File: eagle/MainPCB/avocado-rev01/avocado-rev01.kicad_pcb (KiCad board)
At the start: 2 copper layers, 61.5 x 60 mm, 85 parts, among them J1 10118194-0001LF, J3 0475710001, P2 camconn, U1 V3S, U2 AP65111A, U3 AP65111A, U4 AP65111A, X1 XTAL3.2X2, X2 XTAL5X1.9

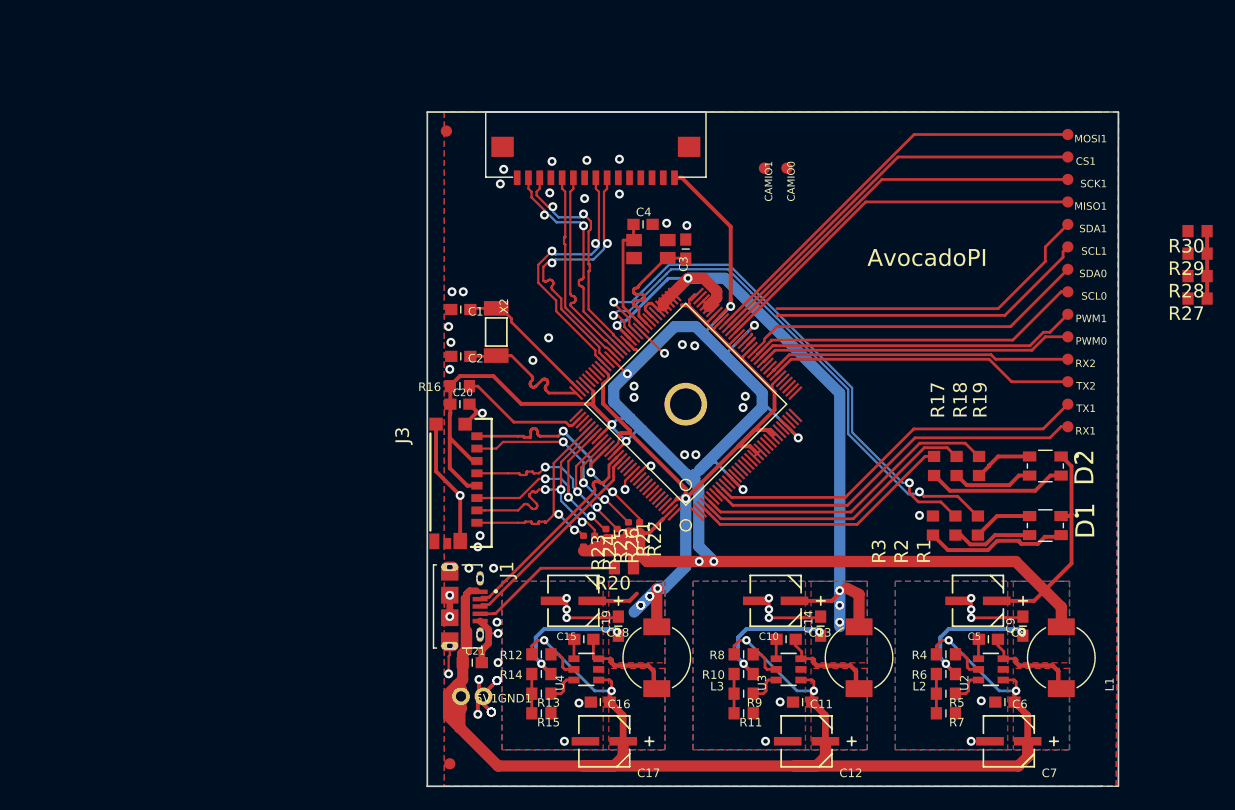
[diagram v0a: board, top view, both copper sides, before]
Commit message: accurate high speed routing, now 4 layer
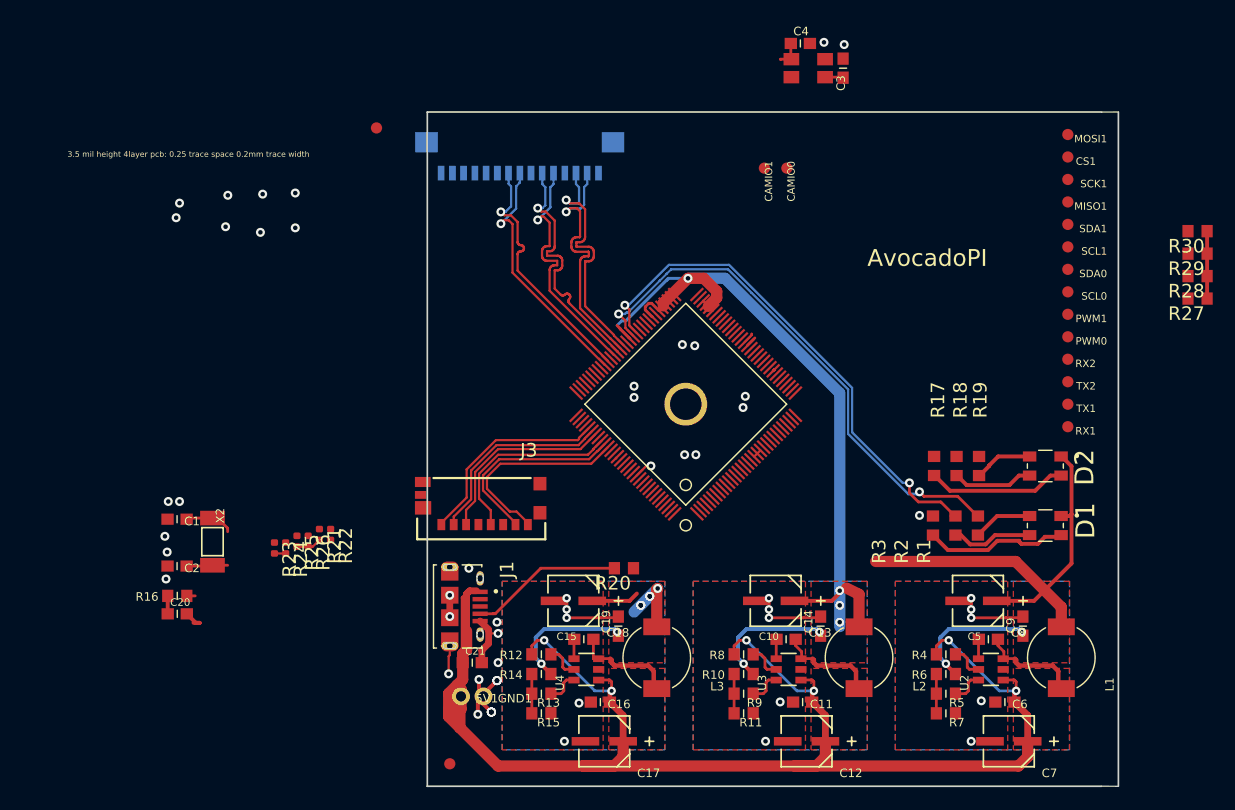
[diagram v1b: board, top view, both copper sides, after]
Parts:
- P2: moved to B.Cu
- moved C1 31.4 mm to (96.2, 111.2)
- moved C2 31.4 mm to (96.2, 115.4)
- moved X2 31.4 mm to (99.4, 113.2)
- moved C20 31.3 mm to (96.2, 119.7)
- moved R16 31.3 mm to (96.2, 118.1)
- moved R21 27.5 mm to (108.9, 112.6)
- moved R22 27.5 mm to (109.9, 112.6)
- moved R23 27.5 mm to (104.9, 113.8)
- moved R24 27.5 mm to (105.9, 113.8)
- moved R25 27.5 mm to (106.9, 113.2)
- moved R26 27.5 mm to (107.9, 113.2)
- moved C3 21.3 mm to (155.5, 71.1)
- moved X1 21.3 mm to (152.4, 71.1)
- moved C4 21.3 mm to (151.7, 68.9)
- moved P2 6.78 mm to (126.7, 77.5), turned to 0 degrees
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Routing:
- net 3V3: track 234.4 -> 61.6 mm, vias 11 -> 2
- net 1V2: track 94.4 -> 23.3 mm, vias 8 -> 7
- net Net-(MOSI1-Pad1): track 37.4 -> 0.00 mm
- net Net-(CS1-Pad1): track 36.4 -> 0.00 mm
- net Net-(SCK1-Pad1): track 35.4 -> 0.00 mm
- net Net-(RX1-Pad1): track 34.7 -> 0.00 mm
- net Net-(TX1-Pad1): track 34.5 -> 0.00 mm
- net Net-(MISO1-Pad1): track 34.4 -> 0.00 mm
- net Net-(R28-Pad2): track 31.1 -> 0.00 mm
- net Net-(R27-Pad2): track 30.0 -> 0.00 mm
- net SDA: track 30.8 -> 1.02 mm
- net Net-(PWM1-Pad1): track 29.0 -> 0.00 mm
- net SCL: track 29.6 -> 0.95 mm
- net Net-(PWM0-Pad1): track 28.0 -> 0.00 mm
- net LED1: track 27.4 -> 0.00 mm
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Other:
- copper layers 2 -> 4
- board text added: "3.5 mil height 4layer pcb: 0.25 trace space 0.2mm trace width"

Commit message: better routing v2
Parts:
- R21, R22, R23, R24, R25, R26: footprint Resistor_SMD:R_0402_1005Metric -> avocado-rev01:R0603; moved to B.Cu
- moved FID2 79.1 mm to (175.9, 76.5)
- moved R16 37.6 mm to (130.2, 102.0), turned to 90 degrees
- moved C2 37.4 mm to (118.5, 85.4), turned to 90 degrees
- moved C1 37.0 mm to (122.7, 85.4), turned to 90 degrees
- moved X2 32.6 mm to (120.7, 88.5), turned to 0 degrees
- moved R30 27.3 mm to (161.3, 76.5)
- moved CAMIO0 27.2 mm to (123.4, 78.2)
- moved CAMIO1 26.7 mm to (121.9, 78.3)
- moved R29 25.6 mm to (163.3, 78.1)
- moved C20 25.5 mm to (121.1, 113.7), turned to 180 degrees
- moved R28 23.8 mm to (163.6, 85.3)
- moved MOSI1 23.7 mm to (152.0, 79.7), turned to 270 degrees
- moved CS1 21.5 mm to (154.0, 79.7), turned to 270 degrees
- moved R27 21.1 mm to (166.9, 85.3), turned to 0 degrees
- moved SCK1 19.5 mm to (156.0, 79.7), turned to 270 degrees
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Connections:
- net Net-(J1-Pad2) renamed /avocado-rev01_3/USB-
- net Net-(J1-Pad3) renamed /avocado-rev01_3/USB+
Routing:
- net 1V2: track 23.3 -> 119.5 mm, vias 7 -> 8
- net VCC: track 142.0 -> 67.7 mm
- net SCL: track 0.95 -> 67.3 mm, vias 0 -> 1
- net SDA: track 1.02 -> 66.4 mm, vias 0 -> 1
- net Net-(TX1-Pad1): track 0.00 -> 33.6 mm
- net Net-(RX1-Pad1): track 0.00 -> 33.3 mm
- net Net-(R28-Pad2): track 0.00 -> 31.3 mm
- net Net-(R27-Pad2): track 0.00 -> 30.1 mm
- net Net-(PWM1-Pad1): track 0.00 -> 28.2 mm
- net Net-(PWM0-Pad1): track 0.00 -> 27.2 mm
- net LED1: track 0.00 -> 27.1 mm
- net Net-(RX2-Pad1): track 0.36 -> 25.8 mm
- net LED0: track 0.00 -> 25.2 mm
- net Net-(TX2-Pad1): track 0.00 -> 24.7 mm
- net /avocado-rev01_3/USB-: track 0.03 -> 24.4 mm
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- added copper zone on In2.Cu, net 3V3
- added copper zone on In1.Cu, net GND
- added copper zone on F.Cu, net VCC
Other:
- board size 61.5 x 60 mm -> 61.5 x 59.8 mm
- board text added: "100 OHM diff, 50 Ohm Single"

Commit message: better routing v3
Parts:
- moved FID2 0.56 mm to (176.4, 76.3)
- moved FID1 0.40 mm to (118.5, 76.3)
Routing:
- net GND: vias 55 -> 65
- added copper zone on In2.Cu, net GND
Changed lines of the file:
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@@
     (thickness 1.6)
     (drawings 7)
-    (tracks 1583)
+    (tracks 1594)
     (zones 0)
     (modules 85)
@@
     (32 B.Adhes user)
     (33 F.Adhes user)
-    (34 B.Paste user)
+    (34 B.Paste user hide)
     (35 F.Paste user)
     (36 B.SilkS user)
@@
   )
   (module avocado-rev01:FIDUCIAL_1MM (layer Top)
-    (at 118.55 76.7)
+    (at 118.5 76.3)
     (fp_text reference FID1 (at 0 -4.0036) (layer F.SilkS) hide
       (effects (font (size 1.27 1.27) (thickness 0.15)))
@@
   )
   (module avocado-rev01:FIDUCIAL_1MM (layer Top)
-    (at 175.9 76.55)
+    (at 176.4 76.3)
     (fp_text reference FID2 (at 82.95 -60.7) (layer F.SilkS) hide
       (effects (font (size 1.27 1.27) (thickness 0.15)))
@@
     (effects (font (size 1.5 1.5) (thickness 0.3)))
   )
+  (via (at 128.6 110.7) (size 0.8) (drill 0.4) (layers Top Bottom) (net 1))
+  (via (at 128.6 108.1) (size 0.8) (drill 0.4) (layers Top Bottom) (net 1))
   (via (at 166.9011 118.2636) (size 0.7564) (drill 0.35) (layers Top Bottom) (net 1))
   (via (at 166.9011 119.2636) (size 0.7564) (drill 0.35) (layers Top Bottom) (net 1))
@@
   (via (at 135.14 99.78) (size 0.8) (drill 0.4) (layers Top Bottom) (net 1))
   (via (at 135.14 100.92) (size 0.8) (drill 0.4) (layers Top Bottom) (net 1))
+  (segment (start 118.125 110.225) (end 118.125 110.225) (width 0.25) (layer Top) (net 1))
+  (via (at 118.125 110.225) (size 0.8) (drill 0.4) (layers Top Bottom) (net 1))
+  (via (at 117.6 129.6) (size 0.8) (drill 0.4) (layers Top Bottom) (net 1))
+  (via (at 118.5 129.6) (size 0.8) (drill 0.4) (layers Top Bottom) (net 1))
+  (via (at 119 118.5) (size 0.8) (drill 0.4) (layers Top Bottom) (net 1))
+  (via (at 119 118.5) (size 0.8) (drill 0.4) (layers Top Bottom) (net 1))
+  (via (at 135.07 81.72) (size 0.8) (drill 0.4) (layers Top Bottom) (net 1))
+  (via (at 135.85 85) (size 0.8) (drill 0.4) (layers Top Bottom) (net 1))
+  (via (at 122.54 82.1) (size 0.8) (drill 0.4) (layers Top Bottom) (net 1))
   (segment (start 145.8011 122.5136) (end 146.3011 122.0136) (width 0.25) (layer Top) (net 2))
   (via (at 146.9011 122.0136) (size 0.7564) (drill 0.35) (layers Top Bottom) (net 2))
@@
     )
   )
-  (zone (net 0) (net_name "") (layers Top In1.Cu) (hatch edge 0.508)
+  (zone (net 0) (net_name "") (layers Top In1.Cu In2.Cu) (hatch edge 0.508)
     (connect_pads (clearance 0.508))
     (min_thickness 0.254)
@@
       )
     )
+  )
+  (zone (net 0) (net_name "") (layers Top In1.Cu) (hatch edge 0.508)
+    (connect_pads (clearance 0.508))
+    (min_thickness 0.254)
+    (keepout (tracks allowed) (vias allowed) (copperpour not_allowed))
+    (fill (arc_segments 16) (thermal_gap 0.508) (thermal_bridge_width 0.508))
+    (polygon
+      (pts
+        (xy 133.4 102.3) (xy 132 103.7) (xy 135.2 106.9) (xy 136.6 105.4)
+      )
+    )
+  )
+  (zone (net 0) (net_name "") (layer In1.Cu) (hatch edge 0.508)
+    (connect_pads (clearance 0.508))
+    (min_thickness 0.254)
+    (keepout (tracks allowed) (vias allowed) (copperpour not_allowed))
+    (fill (arc_segments 16) (thermal_gap 0.508) (thermal_bridge_width 0.508))
+    (polygon
+      (pts
+        (xy 119 112.4) (xy 128.1 112.4) (xy 128.05 111.1) (xy 118.95 111.1)
+      )
+    )
+  )
+  (zone (net 1) (net_name GND) (layer In2.Cu) (hatch edge 0.508)
+    (connect_pads (clearance 0.508))
+    (min_thickness 0.254)
+    (fill yes (arc_segments 16) (thermal_gap 0.508) (thermal_bridge_width 0.508))
+    (polygon
+      (pts
+        (xy 121.71 81.1) (xy 136.05 81.0775) (xy 136.99 82.8425) (xy 136.73 85.795) (xy 121.66 85.76)
+      )
+    )
+  )
+  (zone (net 0) (net_name "") (layer In2.Cu) (hatch edge 0.508)
+    (connect_pads (clearance 0.508))
+    (min_thickness 0.254)
+    (keepout (tracks allowed) (vias allowed) (copperpour not_allowed))
+    (fill (arc_segments 16) (thermal_gap 0.508) (thermal_bridge_width 0.508))
+    (polygon
+      (pts
+        (xy 136.03 81.075) (xy 137.03 83.385) (xy 136.534623 87.295085) (xy 137.899623 87.030085) (xy 137.992123 81.117585)
+      )
+    )
+  )
+  (zone (net 0) (net_name "") (layer In2.Cu) (hatch edge 0.508)
+    (connect_pads (clearance 0.508))
+    (min_thickness 0.254)
+    (keepout (tracks allowed) (vias allowed) (copperpour not_allowed))
+    (fill (arc_segments 16) (thermal_gap 0.508) (thermal_bridge_width 0.508))
+    (polygon
+      (pts
+        (xy 121.56 80.44) (xy 134.29 80.38) (xy 138.025 80.43) (xy 137.975 81.25) (xy 121.54 81.39)
+        (xy 121.57 80.41) (xy 121.57 80.44)
+      )
+    )
+  )
+  (zone (net 0) (net_name "") (layer In2.Cu) (hatch edge 0.508)
+    (connect_pads (clearance 0.508))
+    (min_thickness 0.254)
+    (keepout (tracks allowed) (vias allowed) (copperpour not_allowed))
+    (fill (arc_segments 16) (thermal_gap 0.508) (thermal_bridge_width 0.508))
+    (polygon
+      (pts
+        (xy 136.58 85.83) (xy 122.13 85.65) (xy 121.95 87.13) (xy 136.6 87.3) (xy 136.58 85.81)
+      )
+    )
+  )
+  (zone (net 0) (net_name "") (layer In2.Cu) (hatch edge 0.508)
+    (connect_pads (clearance 0.508))
+    (min_thickness 0.254)
+    (keepout (tracks allowed) (vias allowed) (copperpour not_allowed))
+    (fill (arc_segments 16) (thermal_gap 0.508) (thermal_bridge_width 0.508))
+    (polygon
+      (pts
+        (xy 121.55 80.41) (xy 120.69 80.42) (xy 120.63 87.07) (xy 122.08 87.13) (xy 122.18 85.54)
+        (xy 121.5 85.54) (xy 121.58 80.41) (xy 121.56 80.41)
+      )
+    )

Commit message: decoupling caps
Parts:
- added C22: 10u, avocado-rev01:C0603, B.Cu at (149.7, 103.3)
- added C23: 10u, avocado-rev01:C0603, B.Cu at (138.4, 113.1)
- added C24: 10u, avocado-rev01:C0603, B.Cu at (143.8, 93.5)
- added C25: 10u, avocado-rev01:C0603, B.Cu at (137.0, 97.4)
- added C26: 10u, avocado-rev01:C0603, B.Cu at (132.1, 99.0)
- added C27: 10u, avocado-rev01:C0603, B.Cu at (145.1, 107.5)
- added C28: 10u, avocado-rev01:C0603, B.Cu at (146.5, 95.6)
- added C29: 10u, avocado-rev01:C0603, F.Cu at (140.7, 89.0)
- added C30: 10u, avocado-rev01:C0603, B.Cu at (141.8, 91.7)
- added C31: 10u, avocado-rev01:C0603, B.Cu at (138.6, 93.3)
- added C32: 10u, avocado-rev01:C0603, B.Cu at (138.4, 98.4)
- added C33: 10u, avocado-rev01:C0603, F.Cu at (142.9, 88.5)
- added C34: 10u, avocado-rev01:C0603, B.Cu at (142.2, 105.8)
- added C35: 10u, avocado-rev01:C0603, B.Cu at (145.6, 102.2)
- added C36: 10u, avocado-rev01:C0603, B.Cu at (140.2, 96.3)
- added C37: 10u, avocado-rev01:C0603, B.Cu at (140.2, 104.5)
- added C38: 10u, avocado-rev01:C0603, B.Cu at (138.1, 102.0)
- added C40: 10u, avocado-rev01:C0603, B.Cu at (143.8, 104.2)
- added C41: 10u, avocado-rev01:C0603, B.Cu at (143.5, 97.4)
- added C42: 10u, avocado-rev01:C0603, B.Cu at (145.4, 98.9)
- added C43: 10u, avocado-rev01:C0603, B.Cu at (133.4, 102.5)
- added C44: 10u, avocado-rev01:C0603, B.Cu at (137.0, 105.5)
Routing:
- net GND: track 53.2 -> 149.1 mm, vias 65 -> 86
- net 3V3: track 63.4 -> 78.5 mm
- net 1V2: track 119.5 -> 126.6 mm, vias 8 -> 17
- net SDC0_D1: track 17.1 -> 19.7 mm
- net SDC0_D0: track 17.1 -> 19.8 mm
- net SDC0_CLK: track 18.0 -> 20.6 mm
- net SDC0_CMD: track 17.1 -> 19.2 mm
- net SDC0_D3: track 17.1 -> 19.2 mm
- net SDC0_D2: track 17.1 -> 19.2 mm
- net 1V8: track 90.3 -> 92.2 mm

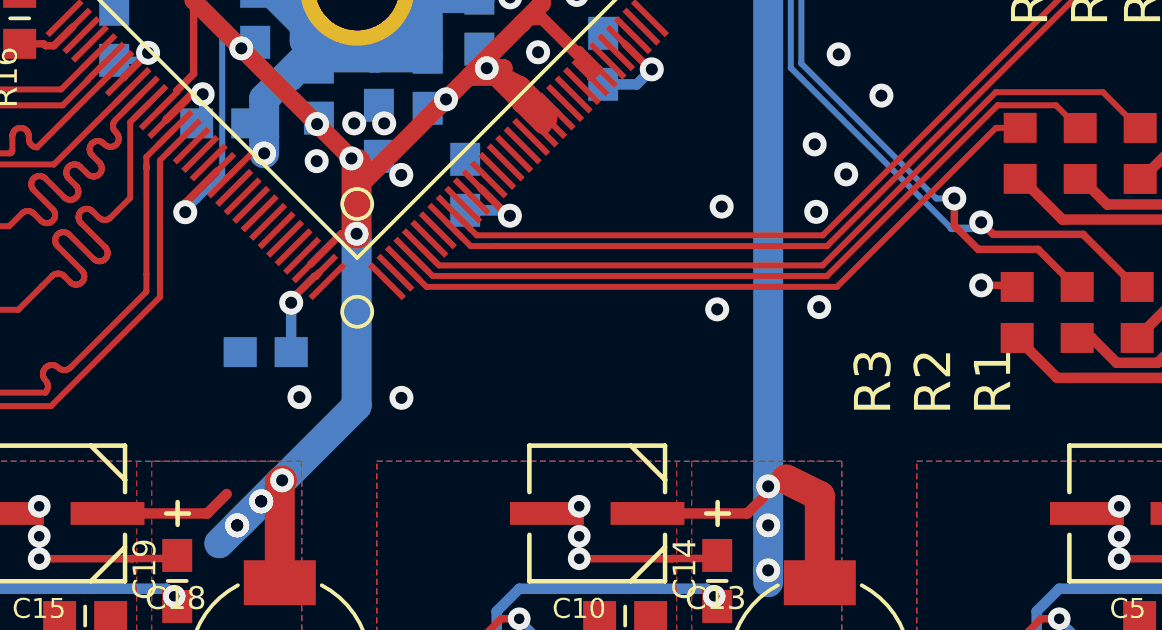
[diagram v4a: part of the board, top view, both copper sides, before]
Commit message: added 3V rail
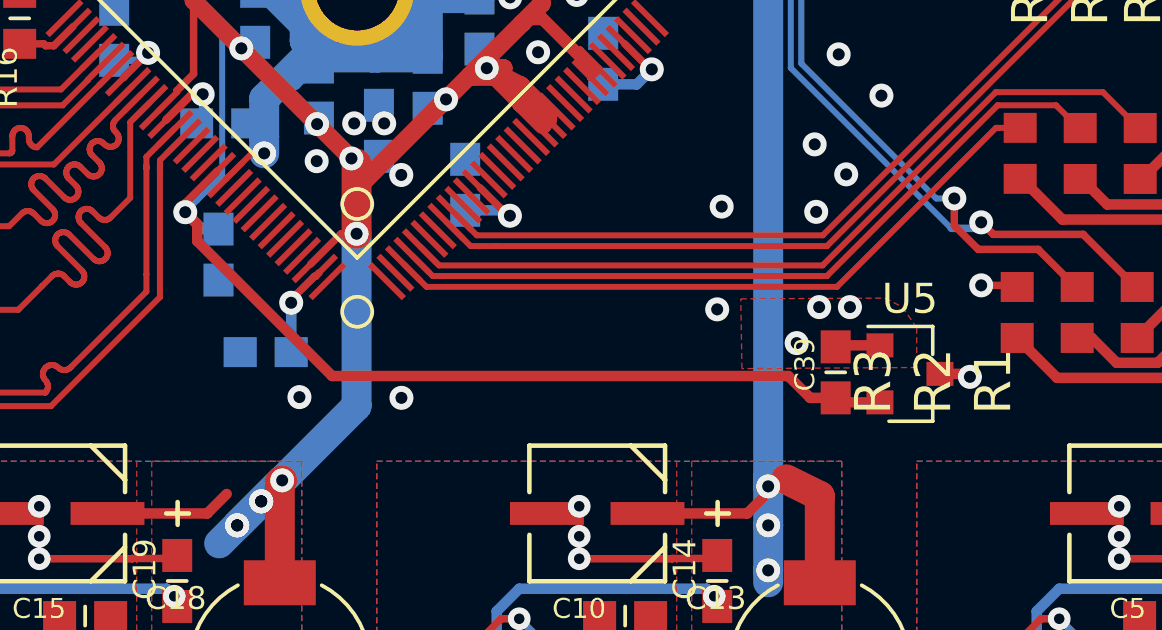
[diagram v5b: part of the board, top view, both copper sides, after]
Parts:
- added C39: 10u, avocado-rev01:C0603, F.Cu at (157.4, 113.8)
- added C45: 10u, avocado-rev01:C0603, B.Cu at (136.9, 109.9)
- added U5: XC6206P302MR, Package_TO_SOT_SMD:SOT-23, F.Cu at (159.9, 113.8)
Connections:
- net /avocado-rev01_4/3V renamed 3V
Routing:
- net 3V: track 18.4 -> 45.8 mm
- net GND: track 149.1 -> 150.5 mm, vias 86 -> 88
- net 3V3: track 78.5 -> 79.5 mm, vias 28 -> 29
